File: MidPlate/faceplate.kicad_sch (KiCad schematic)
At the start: 1 part, among them J12 JST_B4B-XH-A

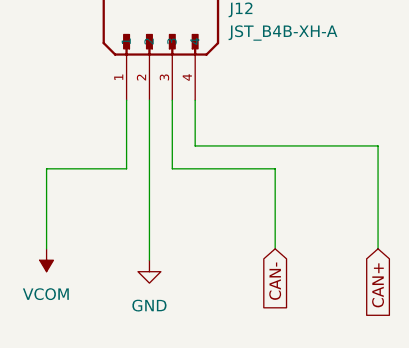
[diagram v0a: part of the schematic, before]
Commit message: midplate updates
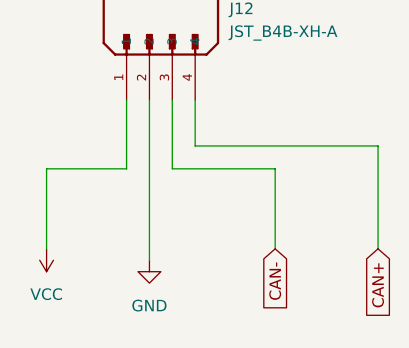
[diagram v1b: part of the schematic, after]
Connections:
- net VCOM renamed VCC
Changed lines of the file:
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@@
-    )
-  )
-  (symbol (lib_id "power:VCOM") (at 86.36 83.82 180) (unit 1)
-    (in_bom yes) (on_board yes) (dnp no) (fields_autoplaced)
-    (property "Reference" "#PWR028" (at 86.36 80.01 0)
-      (effects (font (size 1.27 1.27)) hide)
-    )
-    (property "Value" "VCOM" (at 86.36 88.9 0)
-      (effects (font (size 1.27 1.27)))
-    )
-    (property "Footprint" "" (at 86.36 83.82 0)
-      (effects (font (size 1.27 1.27)) hide)
-    )
-    (property "Datasheet" "" (at 86.36 83.82 0)
-      (effects (font (size 1.27 1.27)) hide)
-    )
-    (pin "1")
-    (instances
-      (project "midplate"
-        (path "/69058343-dac8-421b-a3f6-e069eb1ba8ae/ab54f000-c596-4ae0-81be-92723dd47fdf"
-          (reference "#PWR028") (unit 1)
-        )
-        (path "/69058343-dac8-421b-a3f6-e069eb1ba8ae/e962e4a0-6822-4b24-92cd-4a40d2d1132c"
-          (reference "#PWR024") (unit 1)
-        )
-      )
     )
   )
@@
         )
       )
+    )
+  )
+  (symbol (lib_id "power:VCC") (at 86.36 83.82 180) (unit 1)
+    (in_bom yes) (on_board yes) (dnp no) (fields_autoplaced)
+    (property "Reference" "#PWR04" (at 86.36 80.01 0)
+      (effects (font (size 1.27 1.27)) hide)
+    )
+    (property "Value" "VCC" (at 86.36 88.9 0)
+      (effects (font (size 1.27 1.27)))
+    )
+    (property "Footprint" "" (at 86.36 83.82 0)
+      (effects (font (size 1.27 1.27)) hide)
+    )
+    (property "Datasheet" "" (at 86.36 83.82 0)
+      (effects (font (size 1.27 1.27)) hide)
+    )
+    (pin "1")
+    (instances
+      (project "midplate"
+        (path "/69058343-dac8-421b-a3f6-e069eb1ba8ae/5699b499-0901-4542-927f-3a0270375bb5"
+          (reference "#PWR04") (unit 1)
+        )
+        (path "/69058343-dac8-421b-a3f6-e069eb1ba8ae/e962e4a0-6822-4b24-92cd-4a40d2d1132c"
+          (reference "#PWR011") (unit 1)
+        )
+      )

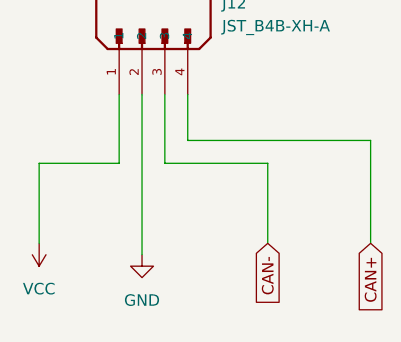
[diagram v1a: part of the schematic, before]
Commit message: midplate 5V buck converter
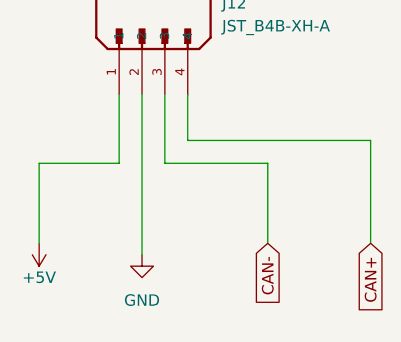
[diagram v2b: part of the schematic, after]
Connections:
- net VCC renamed +5V
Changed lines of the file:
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@@
     )
   )
-  (symbol (lib_id "power:VCC") (at 86.36 83.82 180) (unit 1)
-    (in_bom yes) (on_board yes) (dnp no) (fields_autoplaced)
-    (property "Reference" "#PWR04" (at 86.36 80.01 0)
+  (symbol (lib_id "power:+5V") (at 86.36 83.82 180) (unit 1)
+    (in_bom yes) (on_board yes) (dnp no)
+    (property "Reference" "#PWR013" (at 86.36 80.01 0)
       (effects (font (size 1.27 1.27)) hide)
     )
-    (property "Value" "VCC" (at 86.36 88.9 0)
+    (property "Value" "+5V" (at 86.36 87.63 0)
       (effects (font (size 1.27 1.27)))
     )
@@
     (instances
       (project "midplate"
-        (path "/69058343-dac8-421b-a3f6-e069eb1ba8ae/5699b499-0901-4542-927f-3a0270375bb5"
-          (reference "#PWR04") (unit 1)
+        (path "/69058343-dac8-421b-a3f6-e069eb1ba8ae/ab54f000-c596-4ae0-81be-92723dd47fdf"
+          (reference "#PWR013") (unit 1)
         )
         (path "/69058343-dac8-421b-a3f6-e069eb1ba8ae/e962e4a0-6822-4b24-92cd-4a40d2d1132c"
@@
         )
       )
+      (project "FacePlate"
+        (path "/e63e39d7-6ac0-4ffd-8aa3-1841a4541b55"
+          (reference "#PWR043") (unit 1)
+        )
+      )

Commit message: midplate updates
- pretty close to order: need to verify if we can get 2oz outer copper
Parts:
- removed J12: JST_B4B-XH-A, bots:JST_B4B-XH-A, symbol bots:JST_B4B-XH-A
- added J12: JST_B4B-XH-A, bots:JST_B4B-XH-A, symbol thebots_symlib:JST_B4B-XH-A
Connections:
- net +5V: now also J12.1
- net CAN+: now also J12.4
- net CAN-: now also J12.3
- net GND: now also J12.2
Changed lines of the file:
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@@
+    )
+  )
+  (symbol (lib_id "thebots_symlib:JST_B4B-XH-A") (at 97.79 62.23 90) (unit 1)
+    (in_bom yes) (on_board yes) (dnp no) (fields_autoplaced)
+    (property "Reference" "J12" (at 106.68 57.15 90)
+      (effects (font (size 1.27 1.27)) (justify right))
+    )
+    (property "Value" "JST_B4B-XH-A" (at 106.68 59.69 90)
+      (effects (font (size 1.27 1.27)) (justify right))
+    )
+    (property "Footprint" "bots:JST_B4B-XH-A" (at 97.79 62.23 0)
+      (effects (font (size 1.27 1.27)) (justify bottom) hide)
+    )
+    (property "Datasheet" "" (at 97.79 62.23 0)
+      (effects (font (size 1.27 1.27)) hide)
+    )
+    (property "MPN" "B4B-XH-A(LF)(SN)" (at 97.79 62.23 0)
+      (effects (font (size 1.27 1.27)) (justify bottom) hide)
+    )
+    (property "Manufacturer" "JST Sales America Inc." (at 97.79 62.23 0)
+      (effects (font (size 1.27 1.27)) (justify bottom) hide)
+    )
+    (property "Price" "0.31" (at 97.79 62.23 0)
+      (effects (font (size 1.27 1.27)) hide)
+    )
+    (property "JLC" "" (at 97.79 62.23 0)
+      (effects (font (size 1.27 1.27)) hide)
+    )
+    (property "LCSC" "" (at 97.79 62.23 0)
+      (effects (font (size 1.27 1.27)) hide)
+    )
+    (pin "1")
+    (pin "2")
+    (pin "3")
+    (pin "4")
+    (instances
+      (project "midplate"
+        (path "/69058343-dac8-421b-a3f6-e069eb1ba8ae/e962e4a0-6822-4b24-92cd-4a40d2d1132c"
+          (reference "J12") (unit 1)
+        )
+      )
     )
   )
@@
         )
       )
-    )
-  )
-  (symbol (lib_id "bots:JST_B4B-XH-A") (at 97.79 62.23 90) (unit 1)
-    (in_bom yes) (on_board yes) (dnp no) (fields_autoplaced)
-    (property "Reference" "J12" (at 106.68 57.15 90)
-      (effects (font (size 1.27 1.27)) (justify right))
-    )
-    (property "Value" "JST_B4B-XH-A" (at 106.68 59.69 90)
-      (effects (font (size 1.27 1.27)) (justify right))
-    )
-    (property "Footprint" "bots:JST_B4B-XH-A" (at 97.79 62.23 0)
-      (effects (font (size 1.27 1.27)) (justify bottom) hide)
-    )
-    (property "Datasheet" "" (at 97.79 62.23 0)
-      (effects (font (size 1.27 1.27)) hide)
-    )
-    (property "MPN" "B4B-XH-A(LF)(SN)" (at 97.79 62.23 0)
-      (effects (font (size 1.27 1.27)) (justify bottom) hide)
-    )
-    (property "Manufacturer" "JST Sales America Inc." (at 97.79 62.23 0)
-      (effects (font (size 1.27 1.27)) (justify bottom) hide)
-    )
-    (property "Price" "0.31" (at 97.79 62.23 0)
-      (effects (font (size 1.27 1.27)) hide)
-    )
-    (property "JLC" "" (at 97.79 62.23 0)
-      (effects (font (size 1.27 1.27)) hide)
-    )
-    (property "LCSC" "" (at 97.79 62.23 0)
-      (effects (font (size 1.27 1.27)) hide)
-    )
-    (pin "1")
-    (pin "2")
-    (pin "3")
-    (pin "4")
-    (instances
-      (project "midplate"
-        (path "/69058343-dac8-421b-a3f6-e069eb1ba8ae/e962e4a0-6822-4b24-92cd-4a40d2d1132c"
-          (reference "J12") (unit 1)
-        )
-      )

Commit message: some components files not working. checking a previous midplate branch
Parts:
- J12: symbol thebots_symlib:JST_B4B-XH-A -> bots:JST_B4B-XH-A

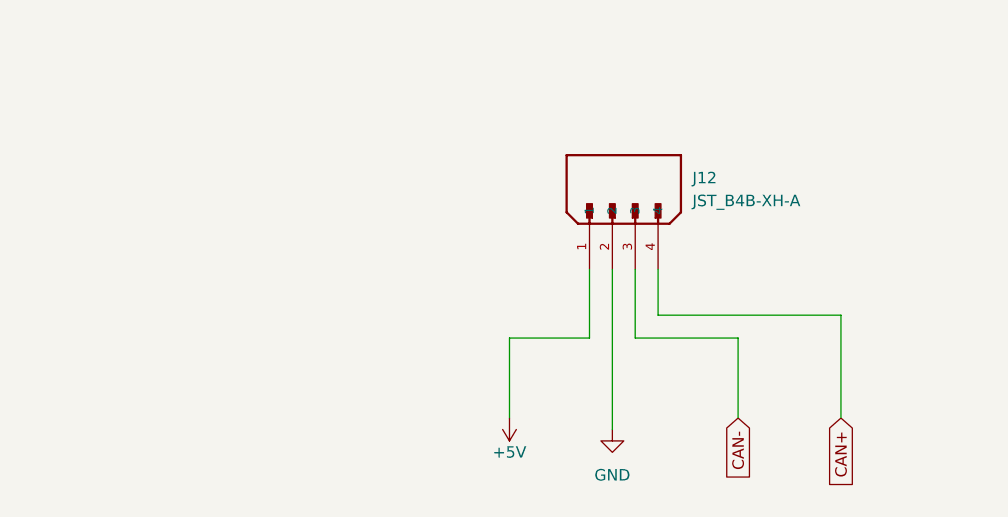
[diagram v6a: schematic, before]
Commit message: add adafruit connector
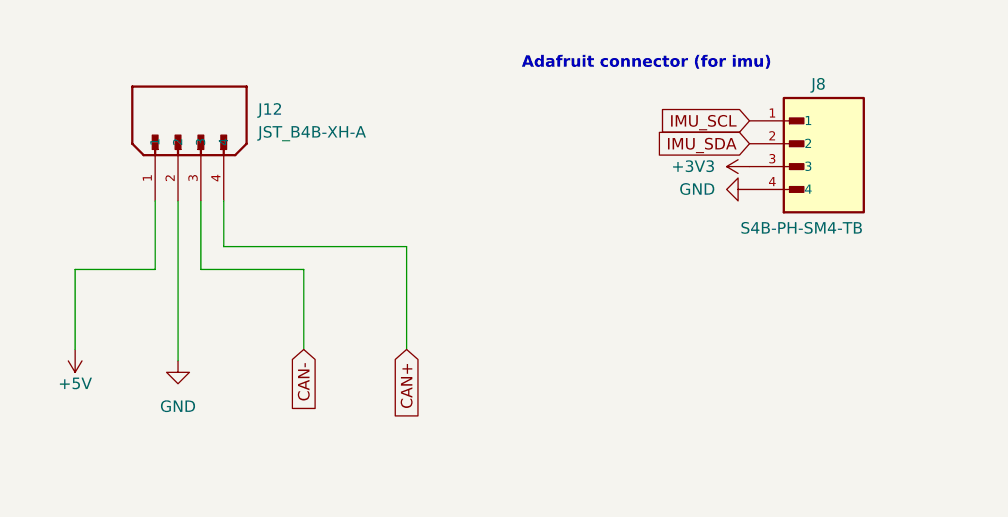
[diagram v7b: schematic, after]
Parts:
- added J8: S4B-PH-SM4-TB, S4B-PH-SM4-TB:JST_S4B-PH-SM4-TB, symbol bots:S4B-PH-SM4-TB
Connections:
- net GND: now also J8.4
- new net +3V3: J8.3
- new net IMU_SCL: J8.1
- new net IMU_SDA: J8.2
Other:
- note added: "Adafruit connector (for imu)"
- moved on the sheet: J12

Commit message: midplate additions WIP
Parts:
- removed J8: S4B-PH-SM4-TB, S4B-PH-SM4-TB:JST_S4B-PH-SM4-TB, symbol bots:S4B-PH-SM4-TB
- added J6: STEMMA_QT, bots:JST_SH_BM04B-SRSS-TB_1x04-1MP_P1.00mm_Vertical, symbol bots:STEMMA_QT
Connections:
- net +3V3: now also J6.2 (Pin_2)
- net GND: now also J6.1 (Pin_1)
- net IMU_SCL: now also J6.4 (Pin_4)
- net IMU_SDA: now also J6.3 (Pin_3)
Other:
- note added: "IMU Connector to faceplate"
- note added: "Power + CAN Connector"
- note removed: "Adafruit connector (for imu)"
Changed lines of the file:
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@@
 	(generator_version "10.0")
 	(paper "A5")
-	(text "Adafruit connector (for imu)"
+	(rectangle
+		(start 31.75 39.37)
+		(end 80.01 87.63)
+		(stroke
+			(width 0)
+			(type default)
+		)
+		(fill
+			(type none)
+		)
+	)
+	(rectangle
+		(start 93.98 39.37)
+		(end 139.7 87.63)
+		(stroke
+			(width 0)
+			(type default)
+		)
+		(fill
+			(type none)
+		)
+	)
+	(text "IMU Connector to faceplate"
 		(exclude_from_sim no)
-		(at 101.6 44.45 0)
+		(at 113.03 44.196 0)
+		(effects
+			(font
+				(size 1.27 1.27)
+				(thickness 0.254)
+				(bold yes)
+			)
+		)
+	)
+	(text "Power + CAN Connector\n"
+		(exclude_from_sim no)
+		(at 56.388 42.672 0)
 		(effects
 			(font
@@
 	)
 	(symbol
-		(lib_id "bots:S4B-PH-SM4-TB")
-		(at 120.65 53.34 0)
-		(unit 1)
-		(body_style 1)
-		(exclude_from_sim no)
-		(in_bom yes)
-		(on_board yes)
-		(in_pos_files yes)
-		(dnp no)
-		(property "Reference" "J8"
-			(at 119.888 46.736 0)
-			(show_name no)
-			(do_not_autoplace no)
-			(effects
-				(font
-					(size 1.27 1.27)
-				)
-				(justify left)
-			)
-		)
-		(property "Value" "S4B-PH-SM4-TB"
-			(at 112.014 62.738 0)
-			(show_name no)
-			(do_not_autoplace no)
-			(effects
-				(font
-					(size 1.27 1.27)
-				)
-				(justify left)
-			)
-		)
-		(property "Footprint" "S4B-PH-SM4-TB:JST_S4B-PH-SM4-TB"
-			(at 120.65 53.34 0)
-			(hide yes)
-			(show_name no)
-			(do_not_autoplace no)
-			(effects
-				(font
-					(size 1.27 1.27)
-				)
-				(justify bottom)
-			)
-		)
-		(property "Datasheet" ""
-			(at 120.65 53.34 0)
-			(hide yes)
-			(show_name no)
-			(do_not_autoplace no)
-			(effects
-				(font
-					(size 1.27 1.27)
-				)
-			)
-		)
-		(property "Description" ""
-			(at 120.65 53.34 0)
-			(hide yes)
-			(show_name no)
-			(do_not_autoplace no)
-			(effects
-				(font
-					(size 1.27 1.27)
-				)
-			)
-		)
-		(property "MF" "JST Sales"
-			(at 120.65 53.34 0)
-			(hide yes)
-			(show_name no)
-			(do_not_autoplace no)
-			(effects
-				(font
-					(size 1.27 1.27)
-				)
-				(justify bottom)
-			)
-		)
-		(property "MAXIMUM_PACKAGE_HEIGHT" "5.5mm"
-			(at 120.65 53.34 0)
-			(hide yes)
-			(show_name no)
-			(do_not_autoplace no)
-			(effects
-				(font
-					(size 1.27 1.27)
-				)
-				(justify bottom)
-			)
-		)
-		(property "CREATOR" "DIZAR"
-			(at 120.65 53.34 0)
-			(hide yes)
-			(show_name no)
-			(do_not_autoplace no)
-			(effects
-				(font
-					(size 1.27 1.27)
-				)
-				(justify bottom)
-			)
-		)
-		(property "Price" "None"
-			(at 120.65 53.34 0)
-			(hide yes)
-			(show_name no)
-			(do_not_autoplace no)
-			(effects
-				(font
-					(size 1.27 1.27)
-				)
-				(justify bottom)
-			)
-		)
-		(property "Package" "None"
-			(at 120.65 53.34 0)
-			(hide yes)
-			(show_name no)
-			(do_not_autoplace no)
-			(effects
-				(font
-					(size 1.27 1.27)
-				)
-				(justify bottom)
-			)
-		)
-		(property "Check_prices" "https://www.snapeda.com/parts/S4B-PH-SM4-TB/JST/view-part/?ref=eda"
-			(at 120.65 53.34 0)
-			(hide yes)
-			(show_name no)
-			(do_not_autoplace no)
-			(effects
-				(font
-					(size 1.27 1.27)
-				)
-				(justify bottom)
-			)
-		)
-		(property "STANDARD" "Manufacturer Recommendations"
-			(at 120.65 53.34 0)
-			(hide yes)
-			(show_name no)
-			(do_not_autoplace no)
-			(effects
-				(font
-					(size 1.27 1.27)
-				)
-				(justify bottom)
-			)
-		)
-		(property "VERIFIER" ""
-			(at 120.65 53.34 0)
-			(hide yes)
-			(show_name no)
-			(do_not_autoplace no)
-			(effects
-				(font
-					(size 1.27 1.27)
-				)
-				(justify bottom)
-			)
-		)
-		(property "SnapEDA_Link" "https://www.snapeda.com/parts/S4B-PH-SM4-TB/JST/view-part/?ref=snap"
-			(at 120.65 53.34 0)
-			(hide yes)
-			(show_name no)
-			(do_not_autoplace no)
-			(effects
-				(font
-					(size 1.27 1.27)
-				)
-				(justify bottom)
-			)
-		)
-		(property "MP" "S4B-PH-SM4-TB"
-			(at 120.65 53.34 0)
-			(hide yes)
-			(show_name no)
-			(do_not_autoplace no)
-			(effects
-				(font
-					(size 1.27 1.27)
-				)
-				(justify bottom)
-			)
-		)
-		(property "Description_1" "Connector Header Surface Mount, Right Angle 4 position 0.079 (2.00mm)"
-			(at 120.65 53.34 0)
-			(hide yes)
-			(show_name no)
-			(do_not_autoplace no)
-			(effects
-				(font
-					(size 1.27 1.27)
-				)
-				(justify bottom)
-			)
-		)
-		(property "Availability" "In Stock"
-			(at 120.65 53.34 0)
-			(hide yes)
-			(show_name no)
-			(do_not_autoplace no)
-			(effects
-				(font
-					(size 1.27 1.27)
-				)
-				(justify bottom)
-			)
-		)
-		(property "MANUFACTURER" "JST Sales"
-			(at 120.65 53.34 0)
-			(hide yes)
-			(show_name no)
-			(do_not_autoplace no)
-			(effects
-				(font
-					(size 1.27 1.27)
-				)
-				(justify bottom)
-			)
-		)
-		(pin "4"
-		)
-		(pin "1"
-		)
-		(pin "2"
-		)
-		(pin "3"
-		)
-		(instances
-			(project "midplate"
-				(path "/69058343-dac8-421b-a3f6-e069eb1ba8ae/e962e4a0-6822-4b24-92cd-4a40d2d1132c"
-					(reference "J8")
-					(unit 1)
-				)
-			)
-		)
-	)
-	(symbol
 		(lib_id "power:+3V3")
 		(at 113.03 55.88 90)
@@
 					(unit 1)
 				)
+			)
+		)
+	)
+	(symbol
+		(lib_id "bots:STEMMA_QT")
+		(at 118.11 55.88 180)
+		(unit 1)
+		(body_style 1)
+		(exclude_from_sim no)
+		(in_bom yes)
+		(on_board yes)
+		(in_pos_files yes)
+		(dnp no)
+		(fields_autoplaced yes)
+		(property "Reference" "J6"
+			(at 123.19 53.9749 0)
+			(show_name no)
+			(do_not_autoplace no)
+			(effects
+				(font
+					(size 1.27 1.27)
+				)
+				(justify right)
+			)
+		)
+		(property "Value" "STEMMA_QT"
+			(at 123.19 56.5149 0)
+			(show_name no)
+			(do_not_autoplace no)
+			(effects
+				(font
+					(size 1.27 1.27)
+				)
+				(justify right)
+			)
+		)
+		(property "Footprint" "bots:JST_SH_BM04B-SRSS-TB_1x04-1MP_P1.00mm_Vertical"
+			(at 118.11 55.88 0)
+			(hide yes)
+			(show_name no)
+			(do_not_autoplace no)
+			(effects
+				(font
+					(size 1.27 1.27)
+				)
+			)
+		)
+		(property "Datasheet" ""
+			(at 118.11 55.88 0)
+			(hide yes)
+			(show_name no)
+			(do_not_autoplace no)
+			(effects
+				(font
+					(size 1.27 1.27)
+				)
+			)
+		)
+		(property "Description" "Generic connector, single row, 01x04, script generated"
+			(at 118.11 55.88 0)
+			(hide yes)
+			(show_name no)
+			(do_not_autoplace no)
+			(effects
+				(font
+					(size 1.27 1.27)
+				)
+			)
+		)
+		(pin "4"
+		)
+		(pin "1"
+		)
+		(pin "2"
+		)
+		(pin "3"
+		)
+		(instances
+			(project "midplate"
+				(path "/69058343-dac8-421b-a3f6-e069eb1ba8ae/e962e4a0-6822-4b24-92cd-4a40d2d1132c"
+					(reference "J6")
+					(unit 1)
+				)
